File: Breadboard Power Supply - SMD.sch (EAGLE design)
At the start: 24 parts, among them J1 POWER_JACKTYLERALT1, U1 V_REG_317SMD

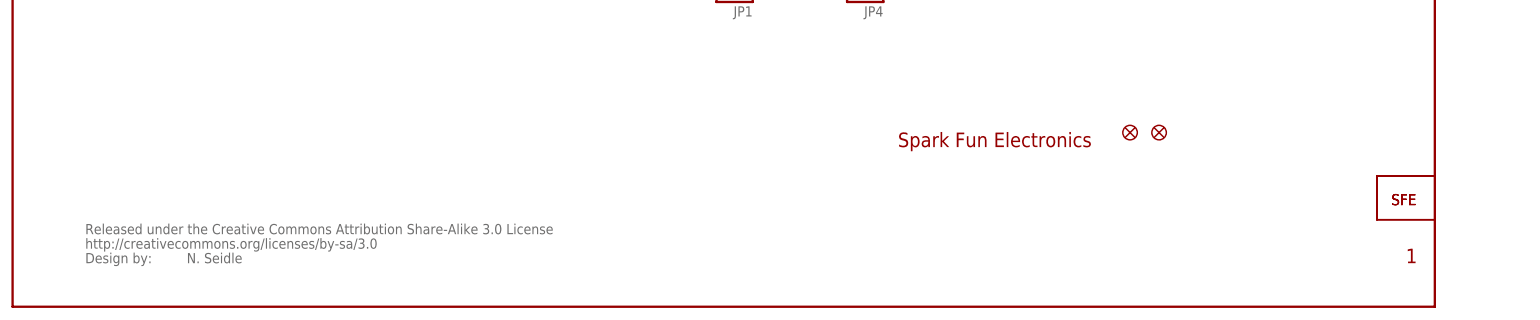
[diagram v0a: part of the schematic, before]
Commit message: Updated frame, rerouted traces, added OSHW
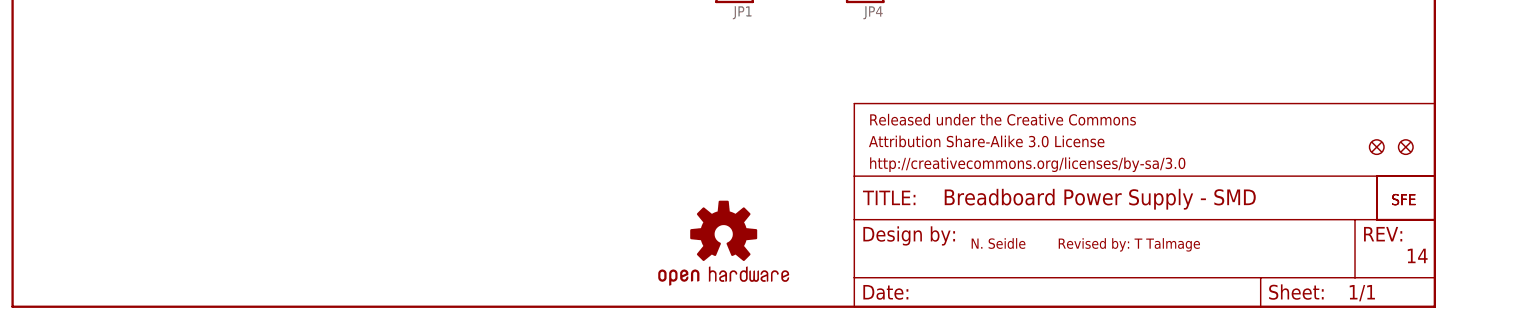
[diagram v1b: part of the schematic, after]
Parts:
- removed U$5: CREATIVE_COMMONS, SparkFun:CREATIVE_COMMONS
- added FRAME1: FRAME-LETTER, SparkFun-Aesthetics:FRAME-LETTER
- added LOGO1: OSHW-LOGOS, SparkFun-Aesthetics:OSHW-LOGOS
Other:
- note added: "14"
- note added: "Revised by: T Talmage"
- note removed: "1"
- note removed: "Spark Fun Electronics"
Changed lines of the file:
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@@
 </classes>
 <parts>
-<part name="FRAME1" library="frames" deviceset="LETTER_L" device=""/>
+<part name="FRAME1" library="SparkFun-Aesthetics" deviceset="FRAME-LETTER" device=""/>
 <part name="R2" library="SparkFun" deviceset="RESISTOR" device="0603-RES" value="390"/>
 <part name="C1" library="SparkFun" deviceset="CAP_POL" device="7343" value="100uF"/>
@@
 <part name="U$3" library="SparkFun" deviceset="FIDUCIAL" device="1X2"/>
 <part name="U$4" library="SparkFun" deviceset="FIDUCIAL" device="1X2"/>
-<part name="U$5" library="SparkFun" deviceset="CREATIVE_COMMONS" device=""/>
+<part name="LOGO1" library="SparkFun-Aesthetics" deviceset="OSHW-LOGO" device="S"/>
 </parts>
 <sheets>
 <sheet>
 <plain>
-<text x="154.94" y="27.94" size="2.54" layer="94">Spark Fun Electronics</text>
-<text x="243.84" y="7.62" size="2.54" layer="94">1</text>
+<text x="243.84" y="7.62" size="2.54" layer="94">14</text>
 <text x="147.32" y="86.36" size="1.778" layer="96">Grounded: 3.3V</text>
 <text x="147.32" y="83.82" size="1.778" layer="96">Open: 5V</text>
-<text x="30.48" y="7.62" size="1.778" layer="95">N. Seidle</text>
+<text x="167.64" y="10.16" size="1.778" layer="94">N. Seidle</text>
 <text x="251.46" y="182.88" size="1.778" layer="94">Changes to v13 (5/23/11):</text>
 <text x="251.46" y="180.34" size="1.778" layer="94">-updated FP on barrel jack to use larger drill holes</text>
@@
 <text x="251.46" y="172.72" size="1.778" layer="94">-changed to 0603 FPs</text>
 <text x="251.46" y="175.26" size="1.778" layer="94">-moved barrel jack up to avoid overhang</text>
+<text x="182.88" y="10.16" size="1.778" layer="94">Revised by: T Talmage</text>
 </plain>
 <instances>
@@
 </instance>
 <instance part="U$2" gate="G$1" x="241.3" y="17.78"/>
-<instance part="U$3" gate="G$1" x="195.58" y="30.48"/>
-<instance part="U$4" gate="G$1" x="200.66" y="30.48"/>
-<instance part="U$5" gate="G$1" x="12.7" y="7.62"/>
+<instance part="U$3" gate="G$1" x="238.76" y="27.94"/>
+<instance part="U$4" gate="G$1" x="243.84" y="27.94"/>
+<instance part="LOGO1" gate="G$1" x="124.46" y="12.7"/>
 </instances>
 <busses>
